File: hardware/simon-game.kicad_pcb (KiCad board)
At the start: 2 copper layers, 50 x 50 mm, 18 parts, among them J1 Conn_01x03_Male, SW1 SW_Push, SW2 SW_Push, SW3 SW_Push, SW4 TACTILE_SW_4Pin, U1 ATtiny402-SS

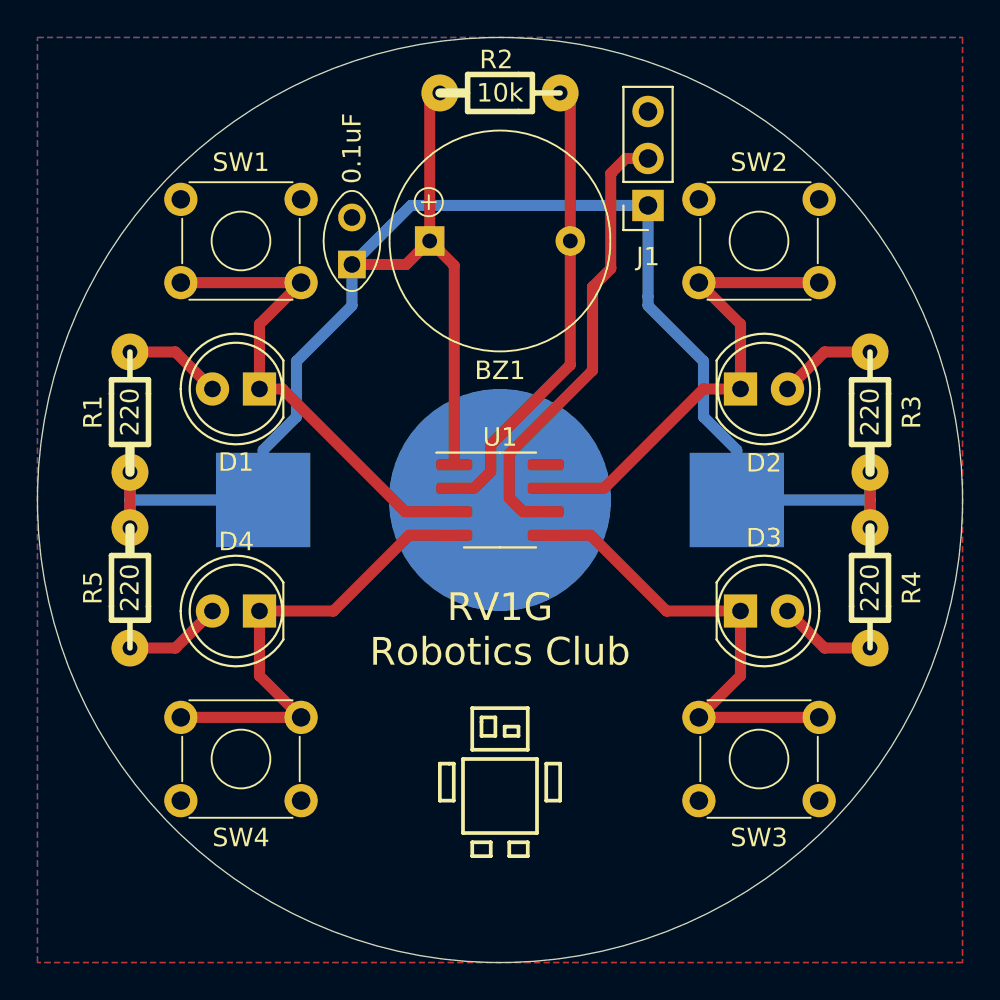
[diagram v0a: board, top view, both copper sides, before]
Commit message: New STM32G030 based hardware
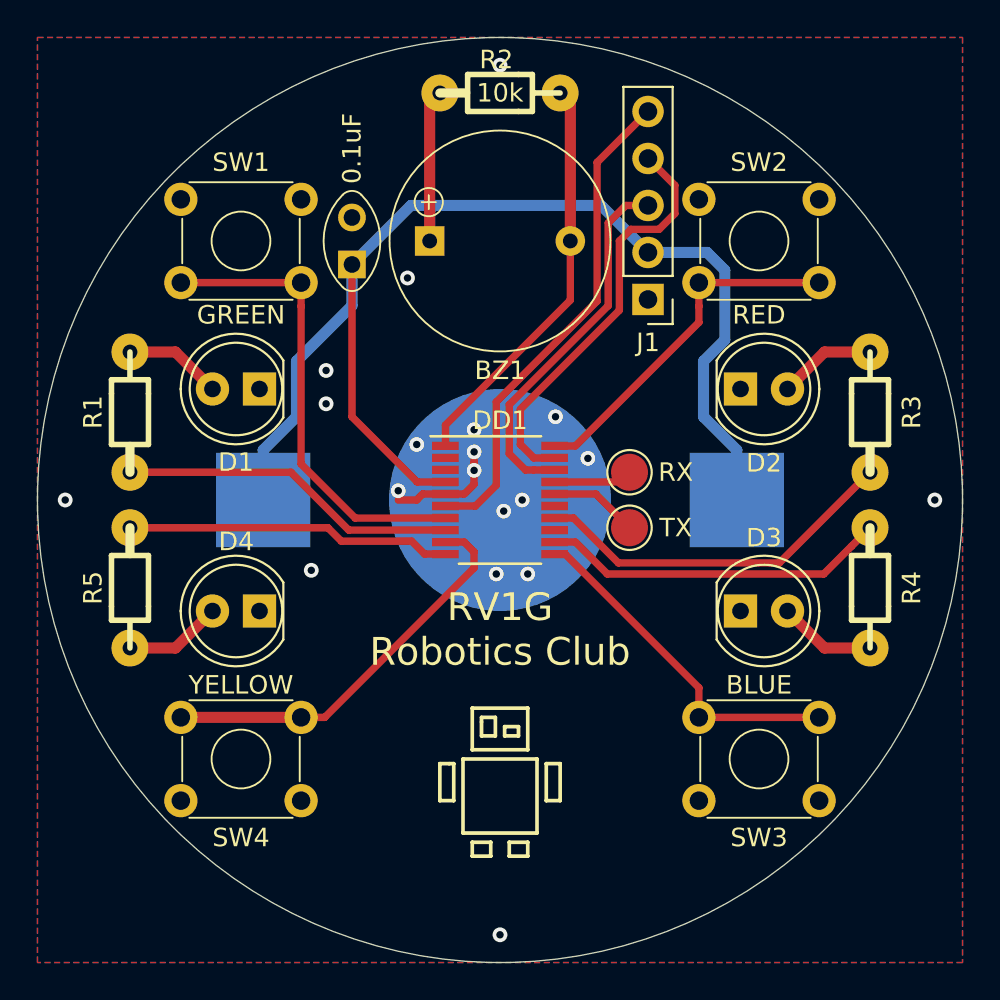
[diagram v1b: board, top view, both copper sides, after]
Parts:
- removed U1: ATtiny402-SS, Package_SO:SOIC-8_3.9x4.9mm_P1.27mm
- added DD1: STM32G030Fxx, Package_SO:TSSOP-20_4.4x6.5mm_P0.65mm, F.Cu at (150.0, 93.0)
- added J2: Conn_01x01, TestPoint:TestPoint_Pad_D2.0mm, F.Cu at (157.0, 94.5)
- added J3: Conn_01x01, TestPoint:TestPoint_Pad_D2.0mm, F.Cu at (157.0, 91.5)
- J1: value Conn_01x03_Male -> Conn_01x05; footprint Connector_PinSocket_2.54mm:PinSocket_1x03_P2.54mm_Vertical -> Connector_PinHeader_2.54mm:PinHeader_1x05_P2.54mm_Vertical
- moved J1 5.08 mm to (158.0, 82.2)
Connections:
- BAT1 pad 1: Net-(BAT1-Pad1) -> VBAT
- BZ1 pad 1: Net-(BAT1-Pad1) -> VBAT
- C1 pad 1: Net-(BAT1-Pad1) -> VBAT
- D1 pad 1: Net-(D1-Pad1) -> GND
- D2 pad 1: Net-(D2-Pad1) -> GND
- D3 pad 1: Net-(D3-Pad1) -> GND
- D4 pad 1: Net-(D4-Pad1) -> GND
- J1 pad 1: Net-(BAT1-Pad1) -> GND
- J1 pad 2: /RESET_UPDI -> VBAT
- J1 pad 3: GND -> /SWDIO
- R1 pad 1: Net-(BAT1-Pad1) -> /LED_GREEN
- R2 pad 1: Net-(BAT1-Pad1) -> VBAT
- R3 pad 1: Net-(BAT1-Pad1) -> /LED_RED
- R4 pad 1: Net-(BAT1-Pad1) -> /LED_BLUE
- R5 pad 1: Net-(BAT1-Pad1) -> /LED_YELLOW
- SW1 pad 1: Net-(D1-Pad1) -> /GREEN
- SW1 pad 2: Net-(D1-Pad1) -> /GREEN
- SW2 pad 1: Net-(D2-Pad1) -> /RED
- SW2 pad 2: Net-(D2-Pad1) -> /RED
- SW3 pad 1: Net-(D3-Pad1) -> /BLUE
- SW3 pad 2: Net-(D3-Pad1) -> /BLUE
- SW4 pad 1: Net-(D4-Pad1) -> /YELLOW
- SW4 pad 2: Net-(D4-Pad1) -> /YELLOW
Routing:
- net Net-(BAT1-Pad1): track 101.9 -> 0.00 mm
- net VBAT: track 0.00 -> 76.3 mm
- net /RESET: track 0.00 -> 26.8 mm
- net Net-(D1-Pad1): track 26.5 -> 0.00 mm
- net Net-(D2-Pad1): track 25.9 -> 0.00 mm
- net Net-(D4-Pad1): track 25.4 -> 0.00 mm
- net Net-(D3-Pad1): track 25.4 -> 0.00 mm
- net /GREEN: track 0.00 -> 25.3 mm
- net /RESET_UPDI: track 24.4 -> 0.00 mm
- net /SWCLK: track 0.00 -> 22.6 mm
- net /YELLOW: track 0.00 -> 21.8 mm
- net /LED_RED: track 0.00 -> 20.1 mm
- net /SWDIO: track 0.00 -> 20.0 mm
- net /RED: track 0.00 -> 19.2 mm
- net /BLUE: track 0.00 -> 18.9 mm
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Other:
- board text added: "2022"
- board text added: "BLUE"
- board text added: "CR2032"
- board text added: "GREEN"
- board text added: "PROG PORT"
- board text added: "RED"
- board text added: "RST SWC SWD VDD GND"
- board text added: "RX"
- board text added: "TX"
- board text added: "YELLOW"
- board text removed: "2019"
